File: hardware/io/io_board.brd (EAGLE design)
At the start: 167.9 x 122.5 mm, 64 parts, among them IC4 74HCT139N, IC5 74AC06N, IC6 8251A, IC7 MAX232, J1 DIN5, T1 BC847, X2 CRYSTALS-NOGND-CFPX-217

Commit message: PCB project fixed
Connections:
- net IO_RD: now also IC3.8
- net IO_WR: now also IC3.10
- net RD: no longer IC3.8
- net WR: no longer IC3.10
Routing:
- net RD: track 176.6 -> 120.9 mm, vias 4 -> 2
- net WR: track 171.8 -> 123.1 mm
- net IO_WR: track 422.2 -> 455.8 mm, vias 12 -> 14
- net IO_RD: track 433.9 -> 464.0 mm, vias 12 -> 14
- net A1: track 304.8 -> 300.5 mm
- net TIMER_IRQ: track 84.5 -> 83.8 mm
- net HLDA: track 112.1 -> 112.8 mm
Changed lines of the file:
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@@
 <?xml version="1.0" encoding="utf-8"?>
 <!DOCTYPE eagle SYSTEM "eagle.dtd">
-<eagle version="7.2.0">
+<eagle version="7.7.0">
 <drawing>
 <settings>
@@
 <setting verticaltext="up"/>
 </settings>
-<grid distance="25" unitdist="mil" unit="mil" style="lines" multiple="1" display="no" altdistance="5" altunitdist="mil" altunit="mil"/>
+<grid distance="25" unitdist="mil" unit="mil" style="lines" multiple="1" display="no" altdistance="12.5" altunitdist="mil" altunit="mil"/>
 <layers>
 <layer number="1" name="Top" color="4" fill="1" visible="yes" active="yes"/>
@@
 <wire x1="34.29" y1="76.835" x2="35.56" y2="76.835" width="0.4064" layer="16"/>
 <wire x1="35.56" y1="76.835" x2="36.83" y2="75.565" width="0.4064" layer="16"/>
-<via x="59.3725" y="75.565" extent="1-16" drill="0.6" diameter="1.4224" shape="octagon"/>
-<wire x1="59.3725" y1="75.565" x2="59.3725" y2="98.425" width="0.4064" layer="1"/>
-<via x="59.3725" y="98.425" extent="1-16" drill="0.6" diameter="1.4224" shape="octagon"/>
+<via x="45.72" y="75.565" extent="1-16" drill="0.6" diameter="1.4224" shape="octagon"/>
+<wire x1="45.72" y1="75.565" x2="45.72" y2="93.345" width="0.4064" layer="1"/>
+<via x="45.72" y="93.345" extent="1-16" drill="0.6" diameter="1.4224" shape="octagon"/>
 <wire x1="107.95" y1="94.615" x2="113.665" y2="94.615" width="0.4064" layer="16"/>
-<wire x1="59.3725" y1="98.425" x2="69.85" y2="98.425" width="0.4064" layer="16"/>
-<wire x1="69.85" y1="98.425" x2="71.4375" y2="96.8375" width="0.4064" layer="16"/>
 <wire x1="71.4375" y1="96.8375" x2="95.5675" y2="96.8375" width="0.4064" layer="16"/>
 <wire x1="95.5675" y1="96.8375" x2="97.155" y2="98.425" width="0.4064" layer="16"/>
@@
 <wire x1="36.83" y1="75.565" x2="40.64" y2="75.565" width="0.4064" layer="16"/>
 <via x="40.64" y="75.565" extent="1-16" drill="0.6" diameter="1.4224" shape="octagon"/>
-<wire x1="59.3725" y1="75.565" x2="40.64" y2="75.565" width="0.4064" layer="16"/>
+<wire x1="45.72" y1="75.565" x2="40.64" y2="75.565" width="0.4064" layer="16"/>
 <contactref element="CON1" pad="19"/>
 <via x="76.5175" y="29.21" extent="1-16" drill="0.6" diameter="1.4224" shape="octagon"/>
@@
 <wire x1="76.5175" y1="21.32" x2="76.5175" y2="29.21" width="0.4064" layer="16"/>
 <wire x1="76.5175" y1="31.75" x2="40.64" y2="31.75" width="0.4064" layer="16"/>
+<wire x1="45.72" y1="93.345" x2="63.5" y2="93.345" width="0.4064" layer="16"/>
+<wire x1="63.5" y1="93.345" x2="66.04" y2="95.885" width="0.4064" layer="16"/>
+<wire x1="66.04" y1="95.885" x2="70.485" y2="95.885" width="0.4064" layer="16"/>
+<wire x1="70.485" y1="95.885" x2="71.4375" y2="96.8375" width="0.4064" layer="16"/>
 </signal>
 <signal name="A2">
@@
 <wire x1="127.635" y1="41.5925" x2="120.015" y2="49.2125" width="0.4064" layer="16"/>
 <via x="104.14" y="49.2125" extent="1-16" drill="0.6" diameter="1.4224" shape="octagon"/>
-<wire x1="104.14" y1="49.2125" x2="104.14" y2="94.615" width="0.4064" layer="1"/>
-<via x="104.14" y="94.615" extent="1-16" drill="0.6" diameter="1.4224" shape="octagon"/>
+<wire x1="104.14" y1="49.2125" x2="104.14" y2="107.315" width="0.4064" layer="1"/>
+<via x="104.14" y="107.315" extent="1-16" drill="0.6" diameter="1.4224" shape="octagon"/>
 <wire x1="104.14" y1="49.2125" x2="120.015" y2="49.2125" width="0.4064" layer="16"/>
-<contactref element="IC3" pad="8"/>
-<wire x1="53.34" y1="94.615" x2="64.77" y2="94.615" width="0.4064" layer="16"/>
-<wire x1="64.77" y1="94.615" x2="66.04" y2="95.885" width="0.4064" layer="16"/>
-<wire x1="99.695" y1="95.885" x2="100.965" y2="94.615" width="0.4064" layer="16"/>
-<wire x1="100.965" y1="94.615" x2="104.14" y2="94.615" width="0.4064" layer="16"/>
-<wire x1="66.04" y1="95.885" x2="99.695" y2="95.885" width="0.4064" layer="16"/>
-<via x="106.045" y="94.615" extent="1-16" drill="0.6" diameter="1.4224" shape="octagon"/>
-<wire x1="104.14" y1="94.615" x2="106.045" y2="94.615" width="0.4064" layer="16"/>
-<via x="106.045" y="107.315" extent="1-16" drill="0.6" diameter="1.4224" shape="octagon"/>
-<wire x1="106.045" y1="107.315" x2="106.045" y2="94.615" width="0.4064" layer="1"/>
-<wire x1="98.425" y1="107.315" x2="106.045" y2="107.315" width="0.4064" layer="16"/>
+<wire x1="98.425" y1="107.315" x2="104.14" y2="107.315" width="0.4064" layer="16"/>
 </signal>
 <signal name="WR">
@@
 <via x="101.6" y="104.775" extent="1-16" drill="0.6" diameter="1.4224" shape="octagon"/>
 <wire x1="101.6" y1="104.775" x2="98.425" y2="104.775" width="0.4064" layer="16"/>
-<contactref element="IC3" pad="10"/>
-<wire x1="53.34" y1="89.535" x2="63.5" y2="89.535" width="0.4064" layer="16"/>
-<wire x1="63.5" y1="89.535" x2="64.77" y2="90.805" width="0.4064" layer="16"/>
-<wire x1="64.77" y1="90.805" x2="99.695" y2="90.805" width="0.4064" layer="16"/>
-<wire x1="99.695" y1="90.805" x2="100.965" y2="89.535" width="0.4064" layer="16"/>
 <via x="105.41" y="89.535" extent="1-16" drill="0.6" diameter="1.4224" shape="octagon"/>
 <wire x1="101.6" y1="104.775" x2="101.6" y2="89.535" width="0.4064" layer="1"/>
@@
 <wire x1="25.4" y1="53.975" x2="21.59" y2="53.975" width="0.4064" layer="16"/>
 <wire x1="26.67" y1="55.245" x2="44.1325" y2="55.245" width="0.4064" layer="16"/>
-<wire x1="36.83" y1="70.485" x2="45.72" y2="70.485" width="0.4064" layer="16"/>
-<wire x1="62.23" y1="70.485" x2="45.72" y2="70.485" width="0.4064" layer="16"/>
 <contactref element="U$1" pad="2"/>
 <wire x1="158.115" y1="55.245" x2="159.7025" y2="56.8325" width="0.4064" layer="16"/>
@@
 <wire x1="49.53" y1="34.29" x2="50.8" y2="35.56" width="0.4064" layer="16"/>
 <wire x1="50.8" y1="35.56" x2="77.7875" y2="35.56" width="0.4064" layer="16"/>
+<contactref element="IC3" pad="8"/>
+<wire x1="36.83" y1="70.485" x2="45.72" y2="70.485" width="0.4064" layer="16"/>
+<wire x1="45.72" y1="70.485" x2="59.3725" y2="70.485" width="0.4064" layer="16"/>
+<via x="59.3725" y="70.485" extent="1-16" drill="0.6" diameter="1.4224" shape="octagon"/>
+<wire x1="59.3725" y1="70.485" x2="62.23" y2="70.485" width="0.4064" layer="16"/>
+<wire x1="53.34" y1="94.615" x2="59.3725" y2="94.615" width="0.4064" layer="16"/>
+<via x="59.3725" y="94.615" extent="1-16" drill="0.6" diameter="1.4224" shape="octagon"/>
+<wire x1="59.3725" y1="94.615" x2="59.3725" y2="70.485" width="0.4064" layer="1"/>
 </signal>
 <signal name="IO_WR">
@@
 <wire x1="31.75" y1="69.215" x2="31.75" y2="60.325" width="0.4064" layer="1"/>
 <contactref element="U$2" pad="10"/>
-<wire x1="36.83" y1="67.945" x2="59.3725" y2="67.945" width="0.4064" layer="16"/>
 <wire x1="31.75" y1="69.215" x2="34.29" y2="69.215" width="0.4064" layer="16"/>
 <wire x1="25.4" y1="20.32" x2="22.86" y2="20.32" width="0.4064" layer="16"/>
@@
 <wire x1="86.36" y1="29.5275" x2="82.55" y2="29.5275" width="0.4064" layer="16"/>
 <wire x1="82.55" y1="29.5275" x2="77.7875" y2="34.29" width="0.4064" layer="16"/>
+<contactref element="IC3" pad="10"/>
+<wire x1="59.3725" y1="67.945" x2="43.18" y2="67.945" width="0.4064" layer="16"/>
+<via x="43.18" y="67.945" extent="1-16" drill="0.6" diameter="1.4224" shape="octagon"/>
+<wire x1="43.18" y1="67.945" x2="43.18" y2="90.805" width="0.4064" layer="1"/>
+<via x="43.18" y="90.805" extent="1-16" drill="0.6" diameter="1.4224" shape="octagon"/>
+<wire x1="43.18" y1="90.805" x2="50.8" y2="90.805" width="0.4064" layer="16"/>
+<wire x1="50.8" y1="90.805" x2="52.07" y2="89.535" width="0.4064" layer="16"/>
+<wire x1="52.07" y1="89.535" x2="53.34" y2="89.535" width="0.4064" layer="16"/>
+<wire x1="36.83" y1="67.945" x2="43.18" y2="67.945" width="0.4064" layer="16"/>
 </signal>
 <signal name="INTA">
@@
 <wire x1="120.015" y1="50.4825" x2="102.87" y2="50.4825" width="0.4064" layer="16"/>
 <via x="102.87" y="50.4825" extent="1-16" drill="0.6" diameter="1.4224" shape="octagon"/>
-<wire x1="102.87" y1="50.4825" x2="102.87" y2="95.885" width="0.4064" layer="1"/>
-<via x="102.87" y="95.885" extent="1-16" drill="0.6" diameter="1.4224" shape="octagon"/>
-<wire x1="102.87" y1="95.885" x2="100.965" y2="95.885" width="0.4064" layer="16"/>
-<wire x1="100.965" y1="95.885" x2="99.695" y2="97.155" width="0.4064" layer="16"/>
-<wire x1="99.695" y1="97.155" x2="98.425" y2="97.155" width="0.4064" layer="16"/>
+<wire x1="102.87" y1="50.4825" x2="102.87" y2="97.155" width="0.4064" layer="1"/>
+<via x="102.87" y="97.155" extent="1-16" drill="0.6" diameter="1.4224" shape="octagon"/>
+<wire x1="102.87" y1="97.155" x2="98.425" y2="97.155" width="0.4064" layer="16"/>
 </signal>
 <signal name="RESET">
@@
 <wire x1="61.2775" y1="106.045" x2="58.7375" y2="103.505" width="0.4064" layer="16"/>
 <wire x1="58.7375" y1="103.505" x2="52.07" y2="103.505" width="0.4064" layer="16"/>
-<wire x1="52.07" y1="103.505" x2="51.435" y2="102.87" width="0.4064" layer="16"/>
-<wire x1="51.435" y1="102.87" x2="51.435" y2="99.695" width="0.4064" layer="16"/>
-<wire x1="51.435" y1="99.695" x2="50.8" y2="99.06" width="0.4064" layer="16"/>
-<wire x1="50.8" y1="99.06" x2="46.99" y2="99.06" width="0.4064" layer="16"/>
-<via x="46.99" y="99.06" extent="1-16" drill="0.6" diameter="1.4224" shape="octagon"/>
-<wire x1="46.99" y1="99.06" x2="46.99" y2="89.535" width="0.4064" layer="1"/>
+<via x="46.99" y="100.965" extent="1-16" drill="0.6" diameter="1.4224" shape="octagon"/>
+<wire x1="46.99" y1="100.965" x2="46.99" y2="89.535" width="0.4064" layer="1"/>
 <via x="46.99" y="89.535" extent="1-16" drill="0.6" diameter="1.4224" shape="octagon"/>
 <wire x1="46.99" y1="89.535" x2="49.53" y2="89.535" width="0.4064" layer="16"/>
@@
 <via x="79.6925" y="76.835" extent="1-16" drill="0.6" diameter="1.4224" shape="octagon"/>
 <wire x1="79.6925" y1="76.835" x2="77.47" y2="76.835" width="0.6096" layer="16"/>
+<wire x1="46.99" y1="100.965" x2="49.53" y2="100.965" width="0.4064" layer="16"/>
+<wire x1="49.53" y1="100.965" x2="52.07" y2="103.505" width="0.4064" layer="16"/>
 </signal>
 <signal name="TC_8257">

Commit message: PCB fixes
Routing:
- net WR: track 123.1 -> 122.4 mm, vias 4 -> 2
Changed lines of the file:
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@@
 <wire x1="120.015" y1="47.9425" x2="105.41" y2="47.9425" width="0.4064" layer="16"/>
 <via x="105.41" y="47.9425" extent="1-16" drill="0.6" diameter="1.4224" shape="octagon"/>
-<wire x1="105.41" y1="47.9425" x2="105.41" y2="89.535" width="0.4064" layer="1"/>
-<via x="101.6" y="104.775" extent="1-16" drill="0.6" diameter="1.4224" shape="octagon"/>
-<wire x1="101.6" y1="104.775" x2="98.425" y2="104.775" width="0.4064" layer="16"/>
-<via x="105.41" y="89.535" extent="1-16" drill="0.6" diameter="1.4224" shape="octagon"/>
-<wire x1="101.6" y1="104.775" x2="101.6" y2="89.535" width="0.4064" layer="1"/>
-<via x="101.6" y="89.535" extent="1-16" drill="0.6" diameter="1.4224" shape="octagon"/>
-<wire x1="100.965" y1="89.535" x2="101.6" y2="89.535" width="0.4064" layer="16"/>
-<wire x1="101.6" y1="89.535" x2="105.41" y2="89.535" width="0.4064" layer="16"/>
+<wire x1="105.41" y1="47.9425" x2="105.41" y2="104.775" width="0.4064" layer="1"/>
+<wire x1="105.41" y1="104.775" x2="98.425" y2="104.775" width="0.4064" layer="16"/>
+<via x="105.41" y="104.775" extent="1-16" drill="0.6" diameter="1.4224" shape="octagon"/>
 </signal>
 <signal name="A14">

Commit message: Buffer added to D0..D7 lined of CF card
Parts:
- added C26: 100N, rcl:C0603
- added IC11: 74HCT245DW, 74xx-eu:SO20W
- R5: device rcl:R0603 -> rcl:0207/10
- moved D2 13.0 mm to (60.3, 40.0), turned to 225 degrees
- moved R5 7.41 mm to (67.9, 31.8), flipped to the top, turned to 90 degrees
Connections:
- new net CF_D0: CON1.21, IC11.11
- new net CF_D1: CON1.22, IC11.12
- new net CF_D2: CON1.23, IC11.13
- new net CF_D3: CON1.2, IC11.18
- new net CF_D4: CON1.3, IC11.17
- new net CF_D5: CON1.4, IC11.16
- new net CF_D6: CON1.5, IC11.15
- new net CF_D7: CON1.6, IC11.14
- net CF_CS0: now also IC11.19
- net D0: now also IC11.9; no longer CON1.21
- net D1: now also IC11.8; no longer CON1.22
- net D2: now also IC11.7; no longer CON1.23
- net D3: now also IC11.2; no longer CON1.2
- net D4: now also IC11.3; no longer CON1.3
- net D5: now also IC11.4; no longer CON1.4
- net D6: now also IC11.5; no longer CON1.5
- net D7: now also IC11.6; no longer CON1.6
- net GND: now also C26.2, IC11.10
- net IO_RD: now also IC11.1
- net VCC: now also C26.1, IC11.20
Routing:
- net D3: track 396.9 -> 239.9 mm
- net CF_CS0: track 62.8 -> 130.6 mm
- net D4: track 314.2 -> 247.3 mm
- net D7: track 298.6 -> 232.2 mm
- net D5: track 316.9 -> 251.5 mm
- net D6: track 306.7 -> 242.8 mm
- net CF_D3: track 0.00 -> 59.1 mm
- net CF_D4: track 0.00 -> 57.3 mm
- net CF_D5: track 0.00 -> 55.5 mm
- net CF_D6: track 0.00 -> 53.7 mm
- net CF_D7: track 0.00 -> 51.9 mm
- net CF_D0: track 0.00 -> 38.2 mm
- net CF_D1: track 0.00 -> 34.6 mm
- net CF_D2: track 0.00 -> 33.0 mm
- net VCC: track 711.5 -> 732.4 mm
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
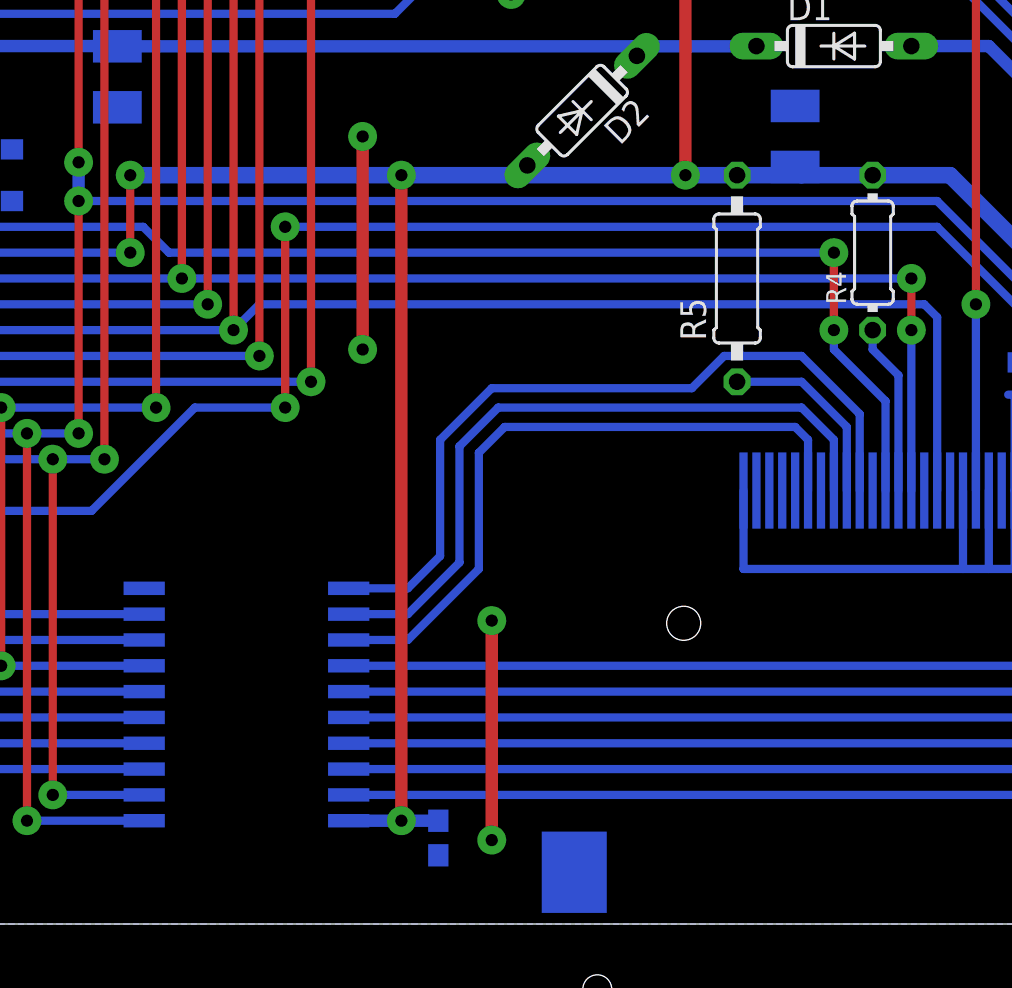
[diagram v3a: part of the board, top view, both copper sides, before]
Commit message: CF indidator LED added to IO board
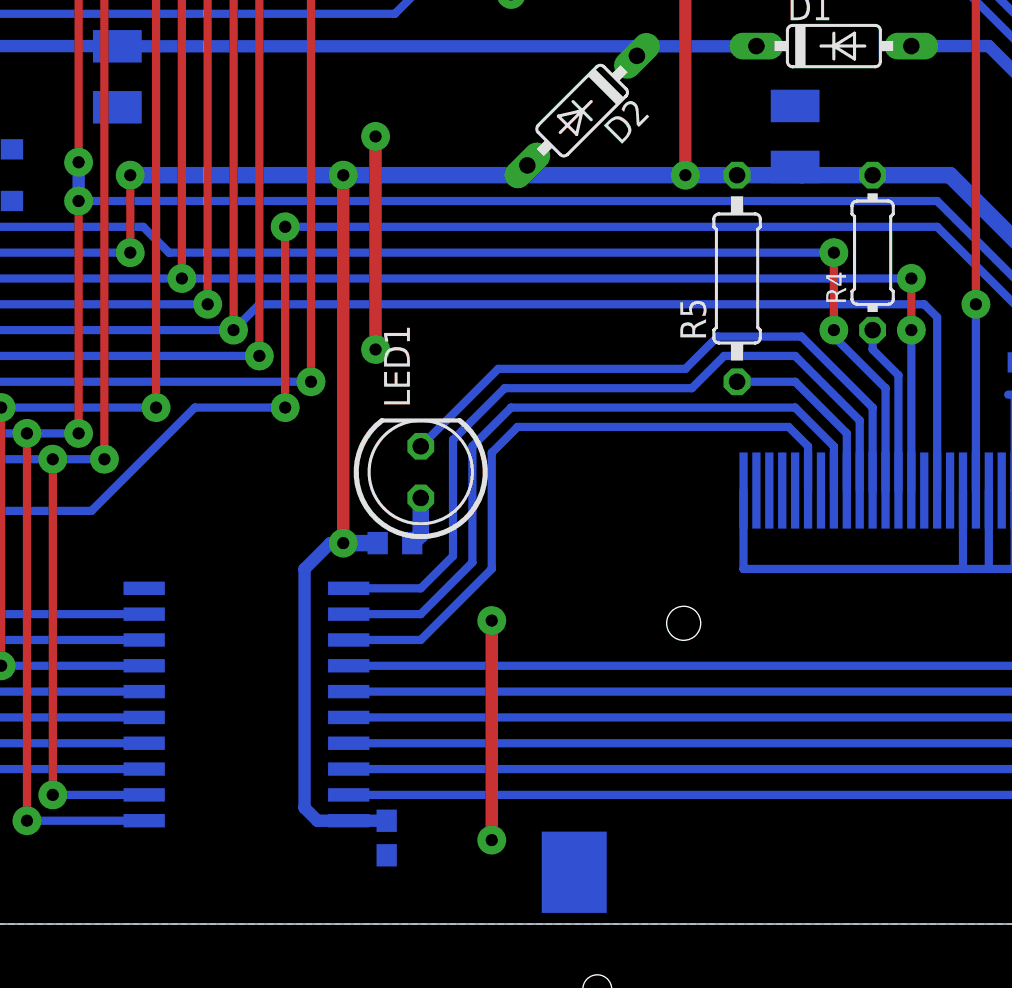
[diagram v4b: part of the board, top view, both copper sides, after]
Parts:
- added LED1: (no value), led:LED5MM
- added R16: (no value), rcl:R0603
- moved C26 2.54 mm to (50.7, 4.23)
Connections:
- new net N$33: CON1.45, LED1.K
- new net N$34: LED1.A, R16.1
- net VCC: now also R16.2
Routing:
- net N$33: track 0.00 -> 30.0 mm
- net N$34: track 0.00 -> 2.40 mm
- net VCC: track 732.4 -> 734.5 mm
